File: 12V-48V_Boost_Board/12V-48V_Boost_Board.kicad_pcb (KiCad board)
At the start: 2 copper layers, 80 x 64 mm, 35 parts, among them J1 12V Input, J2 Input Current Sensing, J3 Output Current Sensing, J4 48V Output, J5 Output Measuring, Q1 FDWS86068-F085

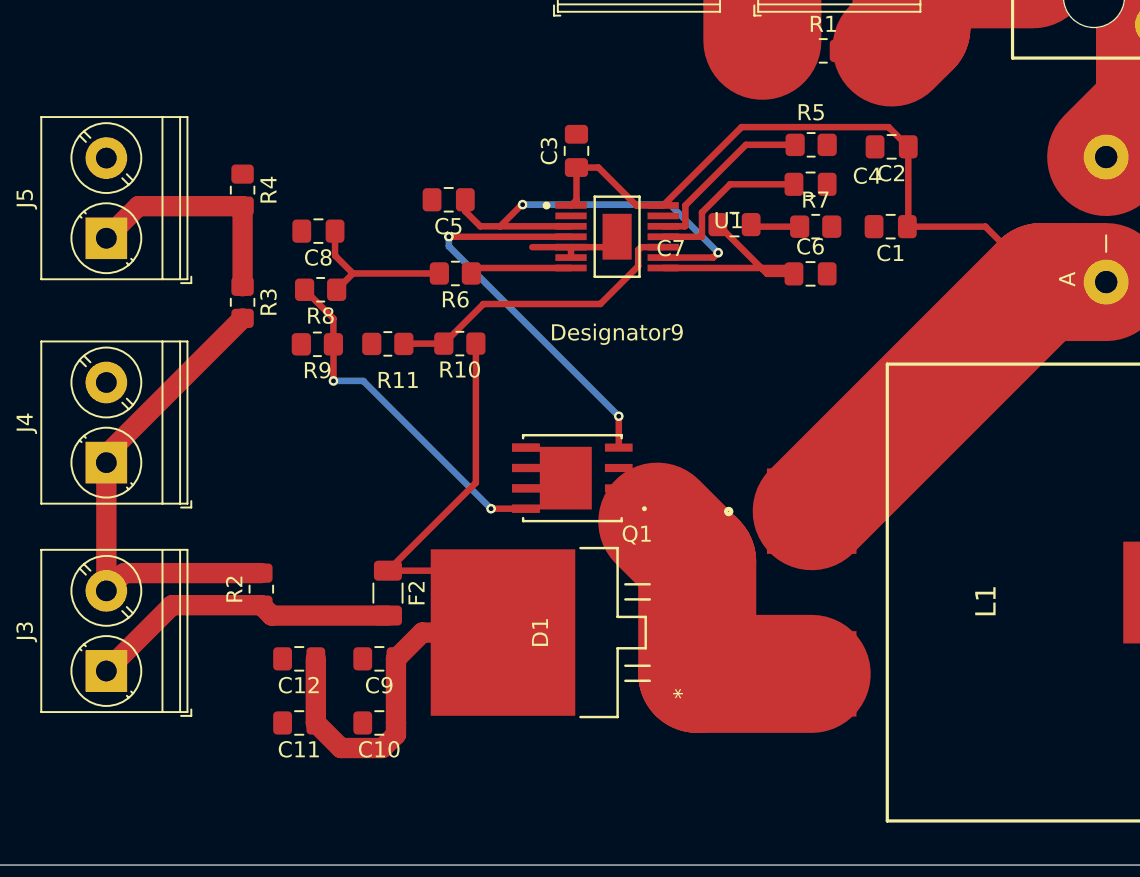
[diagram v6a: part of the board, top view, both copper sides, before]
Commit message: Fixed tracing issues
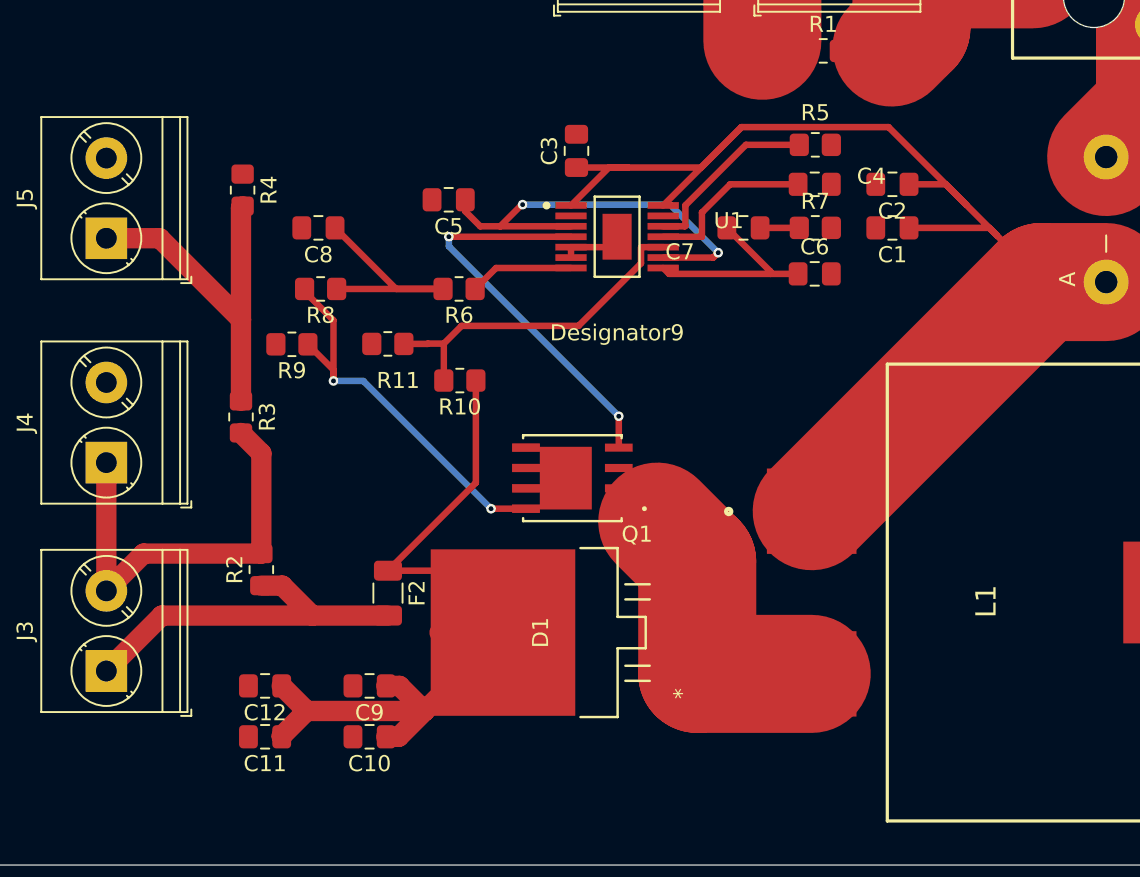
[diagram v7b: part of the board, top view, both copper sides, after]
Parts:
- moved R3 7.15 mm to (138.4, 107.0)
- moved C12 2.72 mm to (139.9, 123.8)
- moved C2 2.34 mm to (179.1, 92.5)
- moved R10 2.30 mm to (152.1, 104.8)
- moved C11 2.30 mm to (139.9, 127.0)
- moved C9 1.79 mm to (146.5, 123.8)
- moved R9 1.59 mm to (141.6, 102.5)
- moved R2 1.22 mm to (139.7, 116.6)
- moved C10 1.06 mm to (146.5, 127.0)
- moved R6 0.99 mm to (152.0, 99.1)
- moved C7 0.59 mm to (169.8, 95.2)
- moved C4 0.26 mm to (174.2, 92.5)
- moved C6 0.26 mm to (174.2, 98.1)
- moved R5 0.26 mm to (174.3, 90.1)
- moved C8 0.20 mm to (143.3, 95.2)
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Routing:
- net /Boost_Board_Chip/12V_INPUT: track 65.7 -> 79.6 mm
- net Net-(J5-Pin_1): track 14.3 -> 22.7 mm
- net Net-(C8-Pad1): track 9.93 -> 15.0 mm
- net /Boost_Board_Chip/48V_OUTPUT: track 41.8 -> 46.7 mm
- net Net-(J3-Pin_2): track 30.1 -> 26.7 mm
- net Net-(J3-Pin_1): track 19.5 -> 22.9 mm
- net Net-(Q1-S): track 21.7 -> 24.7 mm
- net GND: track 5.29 -> 2.88 mm
- net Net-(U1-FB): track 19.2 -> 21.6 mm
- net Net-(U1-COMP): track 13.8 -> 12.6 mm
- net Net-(U1-CS): track 5.87 -> 6.53 mm

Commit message: Minor touchup
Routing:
- net /Boost_Board_Chip/48V_OUTPUT: track 46.7 -> 42.3 mm
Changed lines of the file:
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@@
-	)
-	(segment
-		(start 154.7749 120.4976)
-		(end 154.7749 120.9851)
-		(width 1.27)
-		(layer "F.Cu")
-		(net 8)
 	)
 	(segment
@@
 	)
 	(segment
-		(start 154.7749 120.4976)
-		(end 150.8174 120.4976)
-		(width 1.27)
-		(layer "F.Cu")
-		(net 8)
-	)
-	(segment
 		(start 140.97 126.9514)
 		(end 142.5332 125.3882)
@@
 		(width 0.4064)
 		(layer "F.Cu")
-		(net 16)
-	)
-	(segment
-		(start 142.399 99.219)
-		(end 142.399 99.06)
-		(width 0.4064)
-		(layer "F.Cu")
